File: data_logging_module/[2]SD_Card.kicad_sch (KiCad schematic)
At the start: 12 parts, among them J1 10067847-001RLF

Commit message: Initial scheme
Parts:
- added D201, D202: PESD3V3L1BA,115, Diode_SMD:D_SOD-323, symbol Device:D_TVS
- added R200, R201: 10kR, Resistor_SMD:R_0805_2012Metric, symbol Device:R
- renumbered C4 to C200, C5 to C201, D3 to D200, D4 to D203, D5 to D204, D6 to D205, D7 to D206, J1 to J200, R3 to R202, R4 to R203, R5 to R204, R6 to R205
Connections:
- net +3.3V: now also R200.1, R201.1
- net GND: now also D201.2 (A2), D202.2 (A2)
- net SD_CARD_DAT1: now reaches J200.8 (DAT1)
- net SD_CARD_DAT1: now also D204.1 (A1), R203.2
- net SD_CARD_DAT2: now reaches J200.9 (DAT2)
- net SD_CARD_DAT2: now also D205.1 (A1), R204.2
- net SD_CARD_CD: now reaches J200.CD
- net SD_CARD_WP: now reaches J200.WP
- net SD_CARD_CS renamed SD_CARD_CS/DAT3
- removed net SD_CARD_MISO: D205.1 (A1), J200.7 (DAT0), R204.2
- removed net SD_CARD_MOSI: D204.1 (A1), J200.2 (CMD), R203.2
- net SD_CARD_SCK renamed SD_CARD_DAT0/MISO
- net SD_CARD_DAT0/MISO: now also J200.7 (DAT0); no longer J200.5 (CLK)
- new net SD_CARD_CLK/SCK: D201.1 (A1), J200.5 (CLK), R200.2
- new net SD_CARD_CMD/MOSI: D202.1 (A1), J200.2 (CMD), R201.2
- no-connect marks 4 -> 0
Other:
- moved on the sheet: D200, J200, R202, R203, R204, R205

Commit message: BOM updates
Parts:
- C200: Manufacturer Part Number (none) -> CL21A106KOQNNNE
- C201: Manufacturer Part Number (none) -> CL10B104KB8NNNC
- D200, D201, D202, D203, D204, D205, D206: Manufacturer Part Number (none) -> PESD3V3L1BA,115
- J200: footprint esp32s3_watches:AMPHENOL_10067847-001RLF -> data_logging_module:AMPHENOL_10067847-001RLF; MANUFACTURER Amphenol FCI -> (none); MAXIMUM_PACKAGE_HEIGHT 2.80 mm -> (none); Manufacturer Part Number (none) -> 10067847-001RLF
- R200, R201, R202, R203, R204, R205: Manufacturer Part Number (none) -> 0805W8F1002T5E
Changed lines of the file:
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@@
 			)
 		)
-		(property "Footprint" "esp32s3_watches:AMPHENOL_10067847-001RLF"
+		(property "Footprint" "data_logging_module:AMPHENOL_10067847-001RLF"
 			(at 172.72 73.66 0)
 			(effects
@@
 			)
 		)
-		(property "MANUFACTURER" "Amphenol FCI"
-			(at 172.72 73.66 0)
-			(effects
-				(font
-					(size 1.27 1.27)
-				)
-				(justify bottom)
-				(hide yes)
-			)
-		)
-		(property "MAXIMUM_PACKAGE_HEIGHT" "2.80 mm"
-			(at 172.72 73.66 0)
-			(effects
-				(font
-					(size 1.27 1.27)
-				)
-				(justify bottom)
-				(hide yes)
-			)
-		)
 		(property "STANDARD" "Manufacturer Recommendations"
 			(at 172.72 73.66 0)
@@
 			)
 		)
+		(property "Manufacturer Part Number" "10067847-001RLF"
+			(at 172.72 73.66 0)
+			(effects
+				(font
+					(size 1.27 1.27)
+				)
+				(hide yes)
+			)
+		)
 		(pin "6"
 		)
@@
 		)
 		(property "Manufacturer Product Number" "PESD3V3L1BA,115"
+			(at 87.63 93.98 0)
+			(effects
+				(font
+					(size 1.27 1.27)
+				)
+				(hide yes)
+			)
+		)
+		(property "Manufacturer Part Number" "PESD3V3L1BA,115"
 			(at 87.63 93.98 0)
 			(effects
@@
 			)
 		)
+		(property "Manufacturer Part Number" "0805W8F1002T5E"
+			(at 123.19 57.15 0)
+			(effects
+				(font
+					(size 1.27 1.27)
+				)
+				(hide yes)
+			)
+		)
 		(pin "2"
 		)
@@
 			)
 		)
+		(property "Manufacturer Part Number" "0805W8F1002T5E"
+			(at 87.63 57.15 0)
+			(effects
+				(font
+					(size 1.27 1.27)
+				)
+				(hide yes)
+			)
+		)
 		(pin "2"
 		)
@@
 			)
 		)
+		(property "Manufacturer Part Number" "0805W8F1002T5E"
+			(at 114.3 57.15 0)
+			(effects
+				(font
+					(size 1.27 1.27)
+				)
+				(hide yes)
+			)
+		)
 		(pin "2"
 		)
@@
 		)
 		(property "Manufacturer Product Number" "PESD3V3L1BA,115"
+			(at 105.41 93.98 0)
+			(effects
+				(font
+					(size 1.27 1.27)
+				)
+				(hide yes)
+			)
+		)
+		(property "Manufacturer Part Number" "PESD3V3L1BA,115"
 			(at 105.41 93.98 0)
 			(effects
@@
 			)
 		)
+		(property "Manufacturer Part Number" "CL21A106KOQNNNE"
+			(at 140.97 48.26 0)
+			(effects
+				(font
+					(size 1.27 1.27)
+				)
+				(hide yes)
+			)
+		)
 		(pin "2"
 		)
@@
 		)
 		(property "Manufacturer Product Number" "PESD3V3L1BA,115"
+			(at 114.3 93.98 0)
+			(effects
+				(font
+					(size 1.27 1.27)
+				)
+				(hide yes)
+			)
+		)
+		(property "Manufacturer Part Number" "PESD3V3L1BA,115"
 			(at 114.3 93.98 0)
 			(effects
@@
 			)
 		)
+		(property "Manufacturer Part Number" "0805W8F1002T5E"
+			(at 96.52 57.15 0)
+			(effects
+				(font
+					(size 1.27 1.27)
+				)
+				(hide yes)
+			)
+		)
 		(pin "2"
 		)
@@
 			)
 		)
+		(property "Manufacturer Part Number" "CL10B104KB8NNNC"
+			(at 153.67 48.26 0)
+			(effects
+				(font
+					(size 1.27 1.27)
+				)
+				(hide yes)
+			)
+		)
 		(pin "2"
 		)
@@
 		)
 		(property "Manufacturer Product Number" "PESD3V3L1BA,115"
+			(at 132.08 93.98 0)
+			(effects
+				(font
+					(size 1.27 1.27)
+				)
+				(hide yes)
+			)
+		)
+		(property "Manufacturer Part Number" "PESD3V3L1BA,115"
 			(at 132.08 93.98 0)
 			(effects
@@
 			)
 		)
+		(property "Manufacturer Part Number" "0805W8F1002T5E"
+			(at 132.08 57.15 0)
+			(effects
+				(font
+					(size 1.27 1.27)
+				)
+				(hide yes)
+			)
+		)
 		(pin "2"
 		)
@@
 			)
 		)
+		(property "Manufacturer Part Number" "0805W8F1002T5E"
+			(at 105.41 57.15 0)
+			(effects
+				(font
+					(size 1.27 1.27)
+				)
+				(hide yes)
+			)
+		)
 		(pin "2"
 		)
@@
 		)
 		(property "Manufacturer Product Number" "PESD3V3L1BA,115"
+			(at 123.19 93.98 0)
+			(effects
+				(font
+					(size 1.27 1.27)
+				)
+				(hide yes)
+			)
+		)
+		(property "Manufacturer Part Number" "PESD3V3L1BA,115"
 			(at 123.19 93.98 0)
 			(effects
@@
 			)
 		)
+		(property "Manufacturer Part Number" "PESD3V3L1BA,115"
+			(at 96.52 93.98 0)
+			(effects
+				(font
+					(size 1.27 1.27)
+				)
+				(hide yes)
+			)
+		)
 		(pin "1"
 		)
@@
 			(at 77.47 93.98 0)
 			(effects
+				(font
+					(size 1.27 1.27)
+				)
+				(hide yes)
+			)
+		)
+		(property "Manufacturer Part Number" "PESD3V3L1BA,115"
+			(at 77.47 93.98 0)
+			(effects

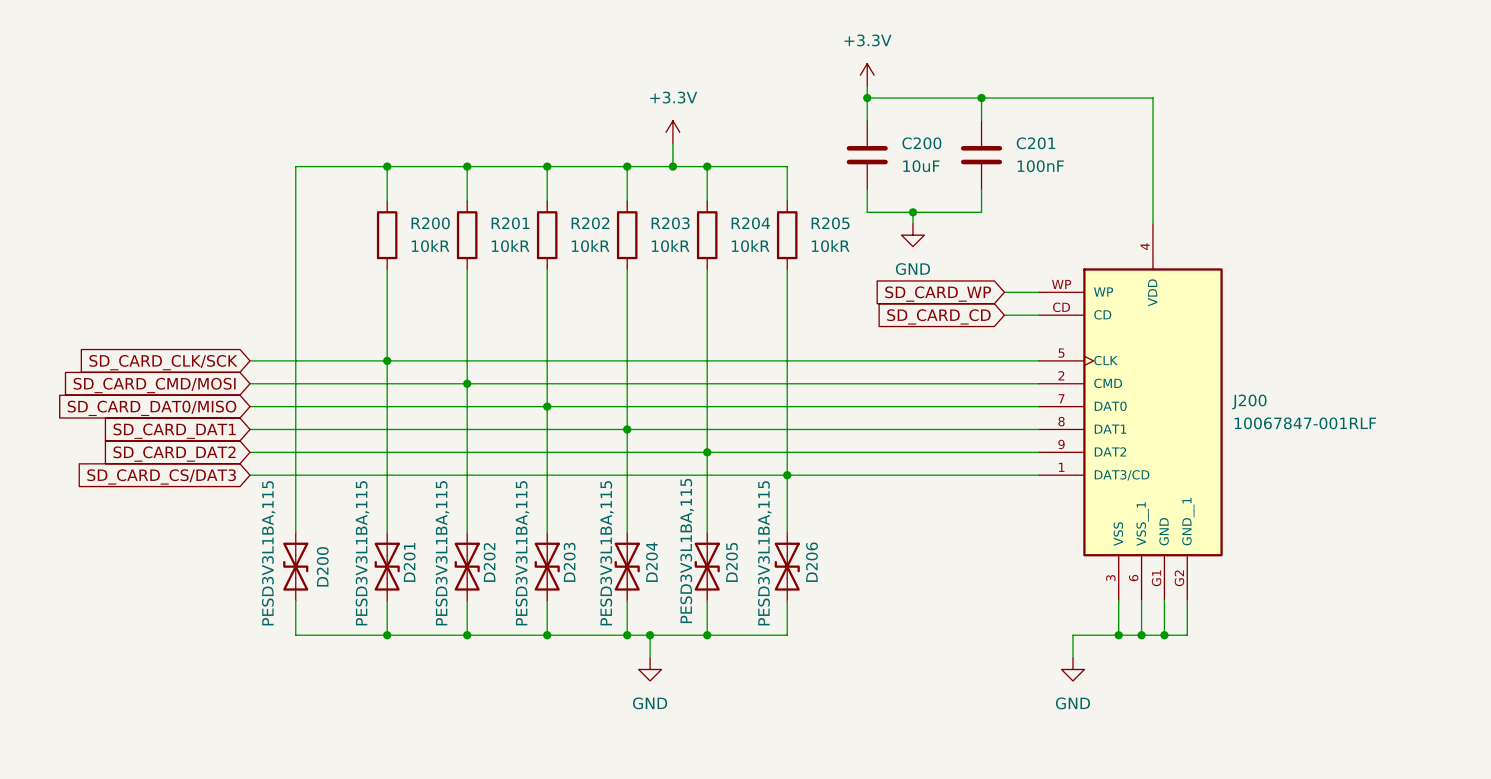
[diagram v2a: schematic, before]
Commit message: Add scheme plots
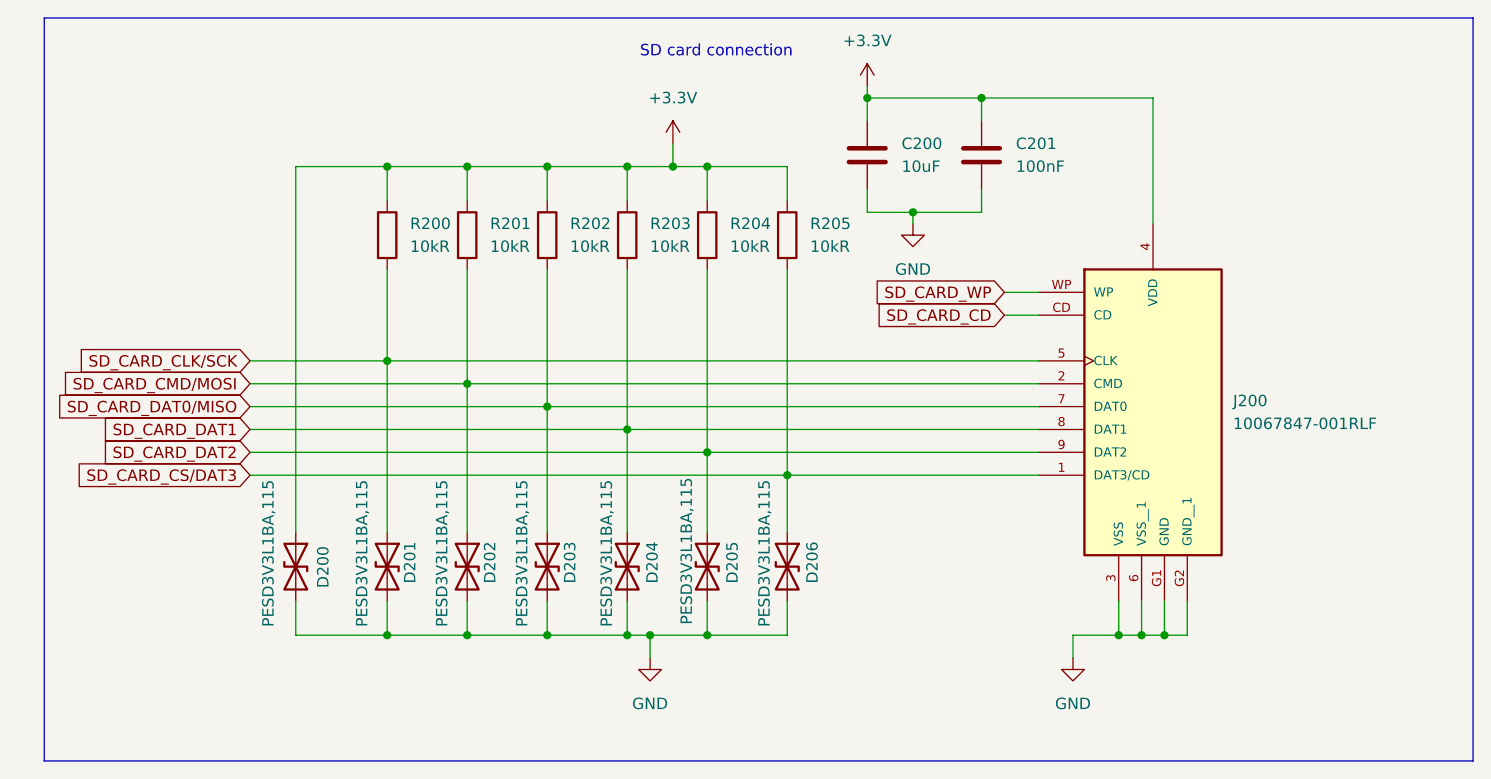
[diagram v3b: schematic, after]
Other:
- note added: "SD card connection"
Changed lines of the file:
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@@
+		)
+	)
+	(rectangle
+		(start 49.53 33.02)
+		(end 208.28 115.57)
+		(stroke
+			(width 0)
+			(type default)
+		)
+		(fill
+			(type none)
+		)
+	)
+	(text "SD card connection"
+		(exclude_from_sim no)
+		(at 124.206 36.83 0)
+		(effects
+			(font
+				(size 1.27 1.27)
+			)
 		)
 	)
